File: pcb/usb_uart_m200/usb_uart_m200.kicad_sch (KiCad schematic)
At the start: 19 parts, among them J1 Conn_01x02_Socket, J6 Conn_01x08_Pin, P1 USB_C_Plug_USB2.0, U1 CY7C65213-28PVXI, U2 MIC5317-3.3xM5, U4 USBLC6-2SC6, X1 2059-301_998-403

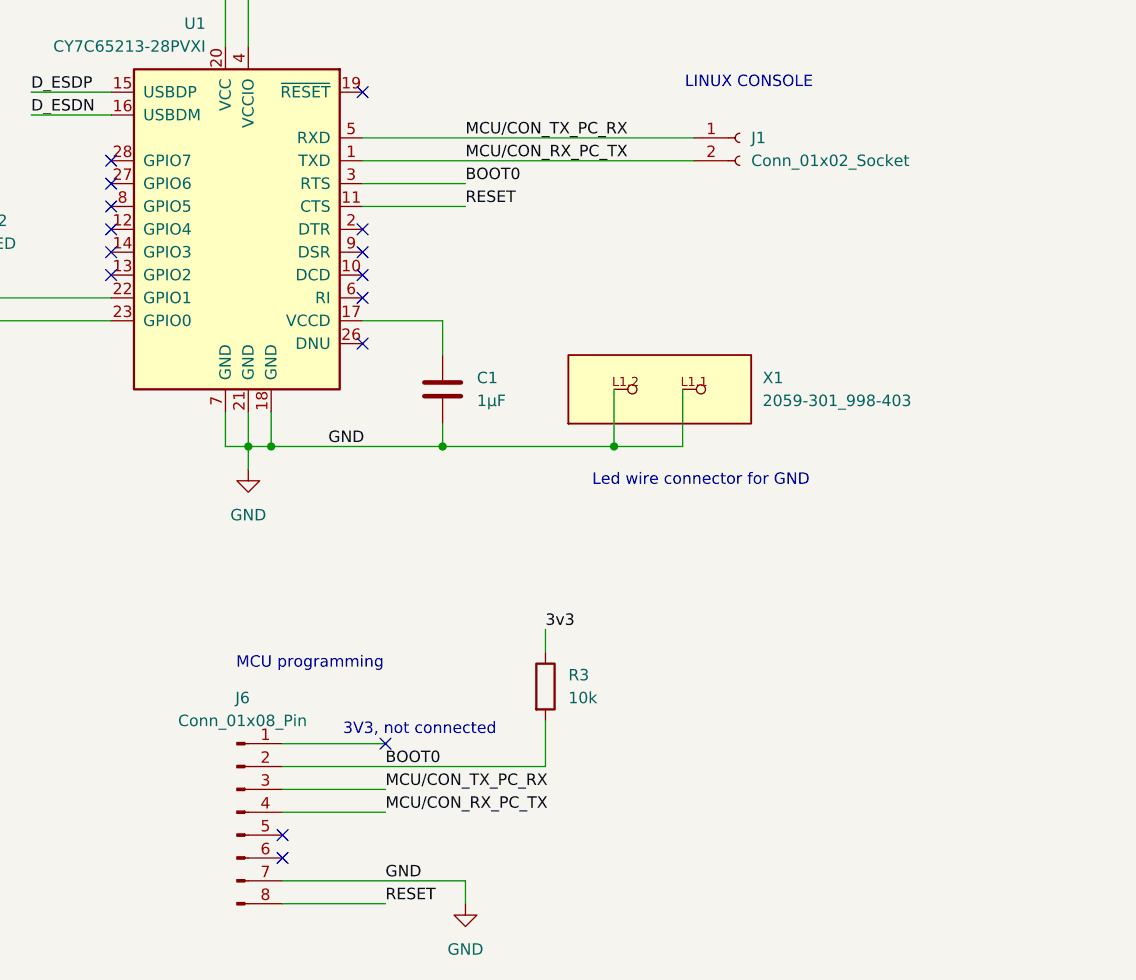
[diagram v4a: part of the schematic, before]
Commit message: Removed the DEBUG header from the serial port board since the MCU needs a stlink total erase.
Adds the screen capture of the configuration in Katapult menuconfig.
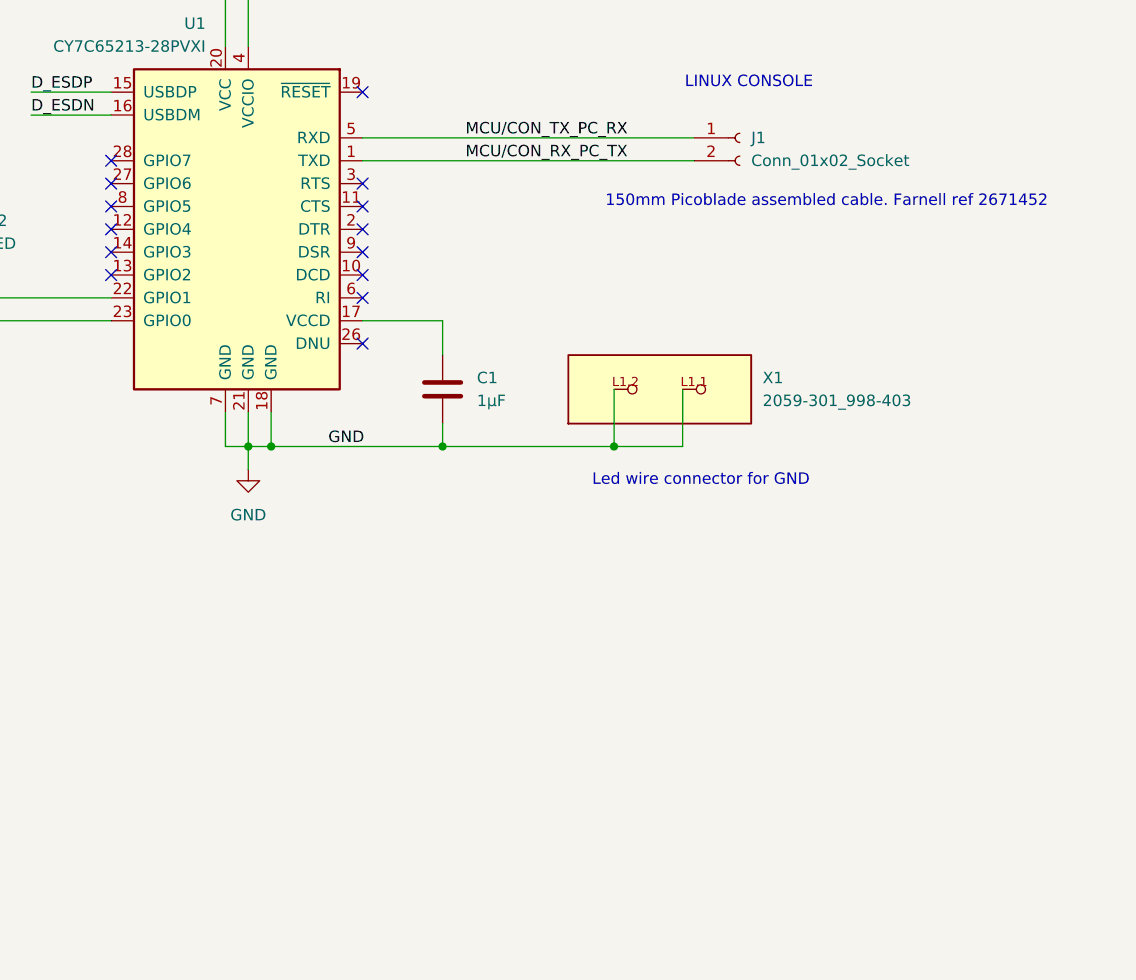
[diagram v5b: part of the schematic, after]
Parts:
- removed J6: Conn_01x08_Pin, Connector_PinHeader_2.54mm:PinHeader_1x08_P2.54mm_Vertical, symbol Connector:Conn_01x08_Pin
- removed R3: 10k, Resistor_SMD:R_0805_2012Metric, symbol Device:R
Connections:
- net BOOT0: no longer names the net of U1.3 (RTS)
- net RESET: no longer names the net of U1.11 (CTS)
- no-connect marks 15 -> 14
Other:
- note added: "150mm Picoblade assembled cable. Farnell ref 2671452"
- note removed: "3V3, not connected"
- note removed: "MCU programming"

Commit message: PCB sources after production
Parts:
- H1, H2: footprint MountingHole:MountingHole_3.2mm_M3_DIN965_Pad_TopBottom -> MountingHole:MountingHole_2.2mm_M2_ISO7380
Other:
- moved on the sheet: H1, H2
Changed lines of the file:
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@@
 	(symbol
 		(lib_id "Mechanical:MountingHole")
-		(at 81.28 130.81 0)
+		(at 54.61 148.59 0)
 		(unit 1)
 		(exclude_from_sim yes)
@@
 		(fields_autoplaced yes)
 		(property "Reference" "H2"
-			(at 83.82 129.5399 0)
+			(at 57.15 147.3199 0)
 			(effects
 				(font
@@
 		)
 		(property "Value" "MountingHole"
-			(at 83.82 132.0799 0)
-			(effects
-				(font
-					(size 1.27 1.27)
-				)
-				(justify left)
-			)
-		)
-		(property "Footprint" "MountingHole:MountingHole_3.2mm_M3_DIN965_Pad_TopBottom"
-			(at 81.28 130.81 0)
+			(at 57.15 149.8599 0)
+			(effects
+				(font
+					(size 1.27 1.27)
+				)
+				(justify left)
+			)
+		)
+		(property "Footprint" "MountingHole:MountingHole_2.2mm_M2_ISO7380"
+			(at 54.61 148.59 0)
 			(effects
 				(font
@@
 		)
 		(property "Datasheet" "~"
-			(at 81.28 130.81 0)
+			(at 54.61 148.59 0)
 			(effects
 				(font
@@
 		)
 		(property "Description" "Mounting Hole without connection"
-			(at 81.28 130.81 0)
+			(at 54.61 148.59 0)
 			(effects
 				(font
@@
 	(symbol
 		(lib_id "Mechanical:MountingHole")
-		(at 81.28 123.19 0)
+		(at 54.61 140.97 0)
 		(unit 1)
 		(exclude_from_sim yes)
@@
 		(fields_autoplaced yes)
 		(property "Reference" "H1"
-			(at 83.82 121.9199 0)
+			(at 57.15 139.6999 0)
 			(effects
 				(font
@@
 		)
 		(property "Value" "MountingHole"
-			(at 83.82 124.4599 0)
-			(effects
-				(font
-					(size 1.27 1.27)
-				)
-				(justify left)
-			)
-		)
-		(property "Footprint" "MountingHole:MountingHole_3.2mm_M3_DIN965_Pad_TopBottom"
-			(at 81.28 123.19 0)
+			(at 57.15 142.2399 0)
+			(effects
+				(font
+					(size 1.27 1.27)
+				)
+				(justify left)
+			)
+		)
+		(property "Footprint" "MountingHole:MountingHole_2.2mm_M2_ISO7380"
+			(at 54.61 140.97 0)
 			(effects
 				(font
@@
 		)
 		(property "Datasheet" "~"
-			(at 81.28 123.19 0)
+			(at 54.61 140.97 0)
 			(effects
 				(font
@@
 		)
 		(property "Description" "Mounting Hole without connection"
-			(at 81.28 123.19 0)
-			(effects
-				(font
+			(at 54.61 140.97 0)
+			(effects
+				(font

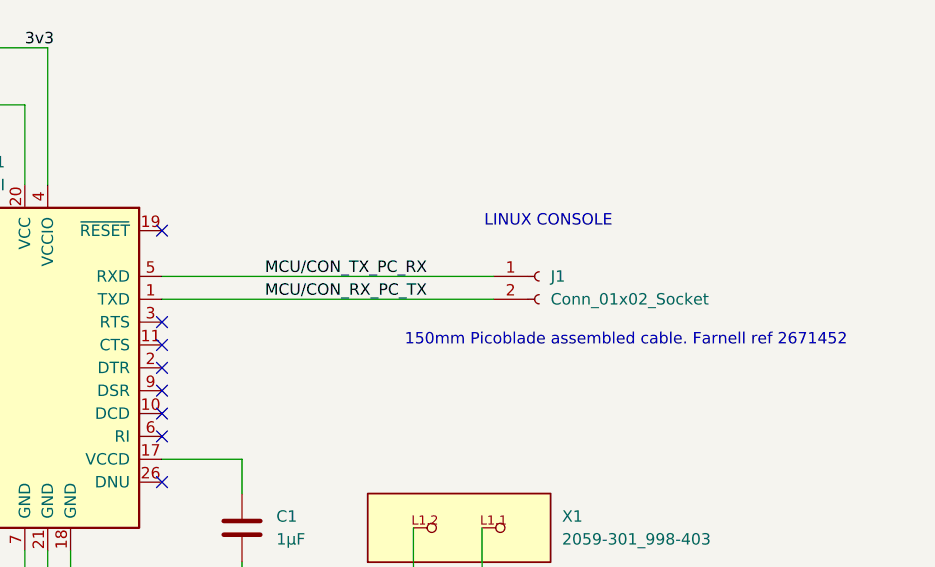
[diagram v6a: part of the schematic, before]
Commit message: Updating the uart and fel mode adapter after soldering it.
Manufacturing shiwed the pcb to be too large and the gnd wire connector
too close to the uart connector. The farnell reference resistor on the
fel mode adapter was of the wrong foorprint.
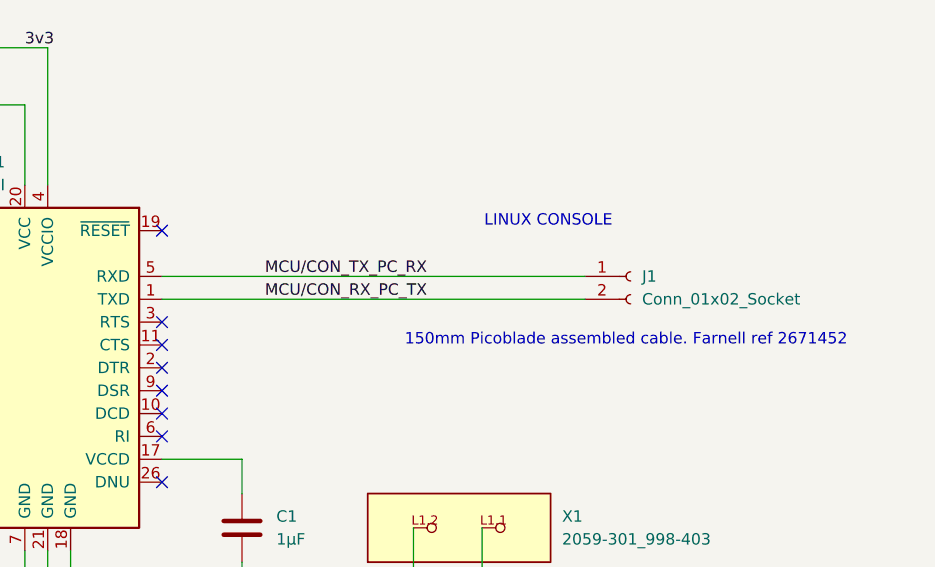
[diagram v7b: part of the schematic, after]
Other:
- moved on the sheet: J1
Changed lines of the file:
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@@
 	(wire
 		(pts
-			(xy 203.2 54.61) (xy 240.03 54.61)
+			(xy 203.2 54.61) (xy 250.19 54.61)
 		)
 		(stroke
@@
 	(wire
 		(pts
-			(xy 203.2 57.15) (xy 240.03 57.15)
+			(xy 203.2 57.15) (xy 250.19 57.15)
 		)
 		(stroke
@@
 	(symbol
 		(lib_id "Connector:Conn_01x02_Socket")
-		(at 245.11 54.61 0)
+		(at 255.27 54.61 0)
 		(unit 1)
 		(exclude_from_sim no)
@@
 		(fields_autoplaced yes)
 		(property "Reference" "J1"
-			(at 246.38 54.6099 0)
+			(at 256.54 54.6099 0)
 			(effects
 				(font
@@
 		)
 		(property "Value" "Conn_01x02_Socket"
-			(at 246.38 57.1499 0)
+			(at 256.54 57.1499 0)
 			(effects
 				(font
@@
 		)
 		(property "Footprint" "Connector_Molex:Molex_PicoBlade_53047-0210_1x02_P1.25mm_Vertical"
-			(at 245.11 54.61 0)
+			(at 255.27 54.61 0)
 			(effects
 				(font
@@
 		)
 		(property "Datasheet" "~"
-			(at 245.11 54.61 0)
+			(at 255.27 54.61 0)
 			(effects
 				(font
@@
 		)
 		(property "Description" "Generic connector, single row, 01x02, script generated"
-			(at 245.11 54.61 0)
+			(at 255.27 54.61 0)
 			(effects
 				(font
@@
 		)
 		(property "farnell" "9733051"
-			(at 245.11 54.61 0)
-			(effects
-				(font
+			(at 255.27 54.61 0)
+			(effects
+				(font
